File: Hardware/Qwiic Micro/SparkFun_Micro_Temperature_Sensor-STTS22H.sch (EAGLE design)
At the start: 27 parts, among them J1 Qwiic Right Angle, U2 STTS22H

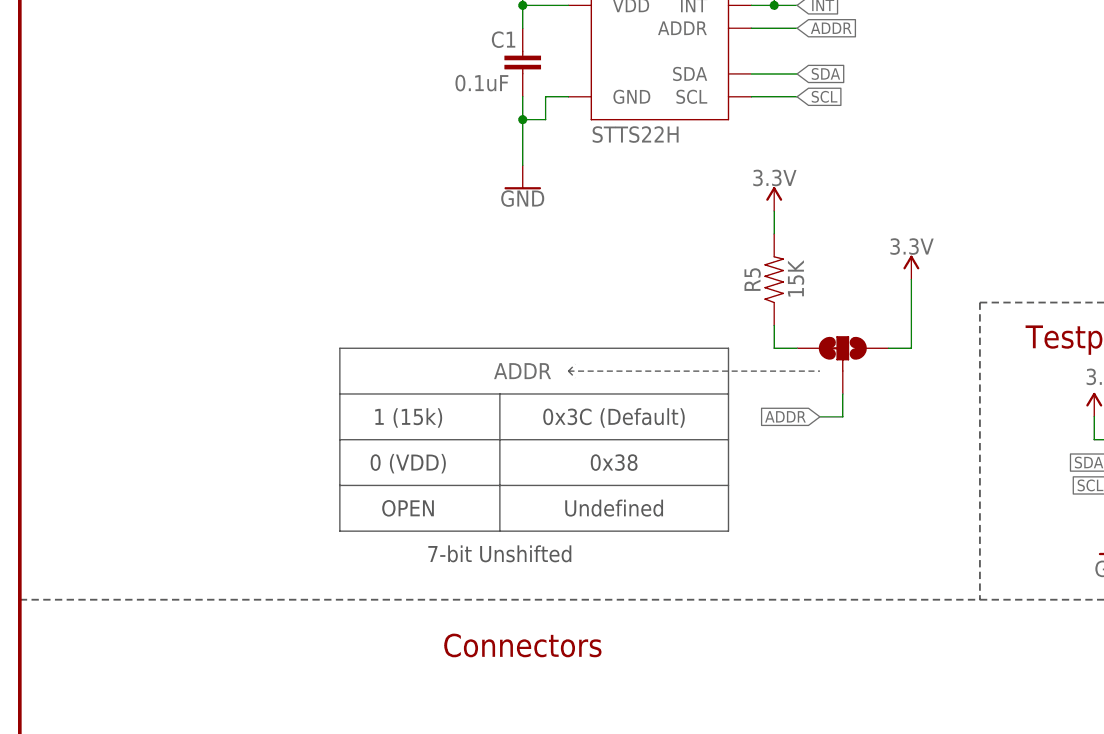
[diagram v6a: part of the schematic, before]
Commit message: Updates address selection text in schematic to be more clear
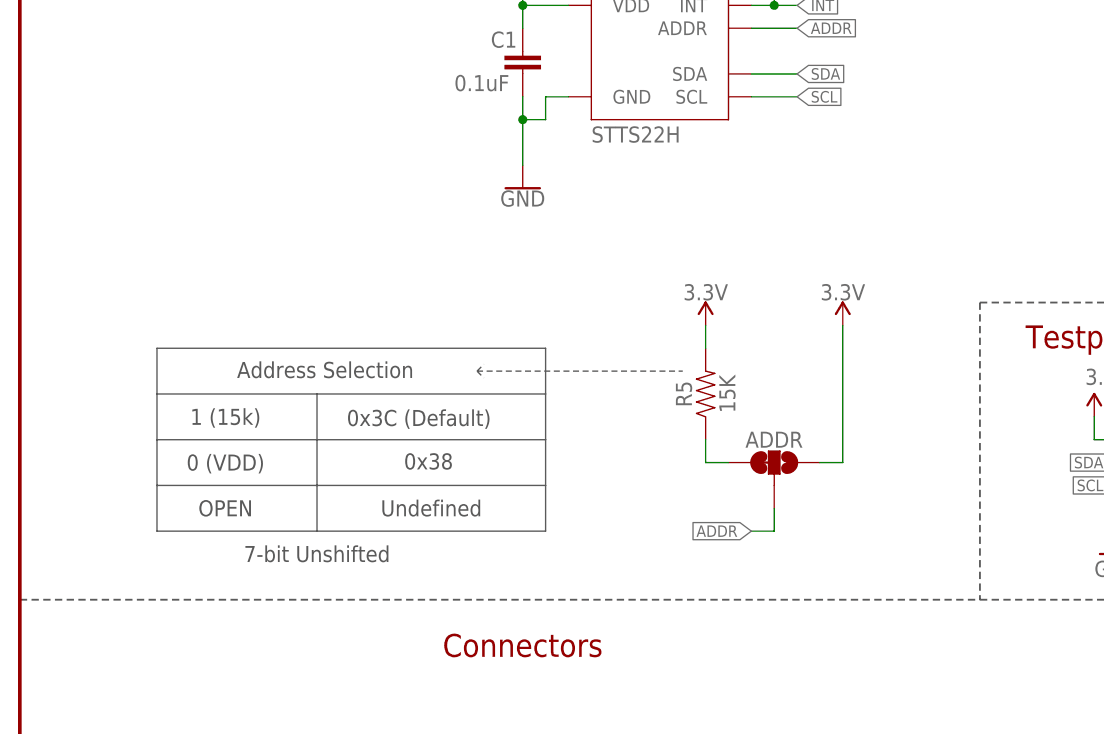
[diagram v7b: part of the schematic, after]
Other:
- note added: "Address Selection"
- moved on the sheet: ADDR, R5
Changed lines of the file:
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@@
 <text x="16.002" y="45.466" size="1.778" layer="97" font="vector">PTH connectors only
 accept 22AWG or smaller</text>
-<wire x1="35.56" y1="104.14" x2="35.56" y2="99.06" width="0.1524" layer="97"/>
-<wire x1="35.56" y1="99.06" x2="35.56" y2="93.98" width="0.1524" layer="97"/>
-<wire x1="35.56" y1="93.98" x2="35.56" y2="88.9" width="0.1524" layer="97"/>
-<wire x1="35.56" y1="88.9" x2="35.56" y2="83.82" width="0.1524" layer="97"/>
-<wire x1="53.34" y1="83.82" x2="78.74" y2="83.82" width="0.1524" layer="97"/>
-<wire x1="78.74" y1="83.82" x2="78.74" y2="88.9" width="0.1524" layer="97"/>
-<wire x1="78.74" y1="88.9" x2="78.74" y2="93.98" width="0.1524" layer="97"/>
-<wire x1="78.74" y1="93.98" x2="78.74" y2="99.06" width="0.1524" layer="97"/>
-<wire x1="78.74" y1="99.06" x2="78.74" y2="104.14" width="0.1524" layer="97"/>
-<wire x1="78.74" y1="104.14" x2="35.56" y2="104.14" width="0.1524" layer="97"/>
-<wire x1="35.56" y1="99.06" x2="53.34" y2="99.06" width="0.1524" layer="97"/>
-<wire x1="53.34" y1="99.06" x2="78.74" y2="99.06" width="0.1524" layer="97"/>
-<wire x1="53.34" y1="99.06" x2="53.34" y2="93.98" width="0.1524" layer="97"/>
-<wire x1="53.34" y1="93.98" x2="53.34" y2="88.9" width="0.1524" layer="97"/>
-<wire x1="53.34" y1="88.9" x2="53.34" y2="83.82" width="0.1524" layer="97"/>
-<wire x1="35.56" y1="88.9" x2="53.34" y2="88.9" width="0.1524" layer="97"/>
-<wire x1="35.56" y1="83.82" x2="53.34" y2="83.82" width="0.1524" layer="97"/>
-<wire x1="53.34" y1="88.9" x2="78.74" y2="88.9" width="0.1524" layer="97"/>
-<text x="43.18" y="96.52" size="1.778" layer="97" font="vector" align="center">1 (15k)</text>
-<text x="43.18" y="91.44" size="1.778" layer="97" font="vector" align="center">0 (VDD)</text>
-<text x="43.18" y="86.36" size="1.778" layer="97" font="vector" align="center">OPEN</text>
-<text x="66.04" y="86.36" size="1.778" layer="97" font="vector" align="center">Undefined</text>
-<text x="53.34" y="81.28" size="1.778" layer="97" font="vector" align="center">7-bit Unshifted</text>
-<wire x1="35.56" y1="93.98" x2="53.34" y2="93.98" width="0.1524" layer="97"/>
-<wire x1="53.34" y1="93.98" x2="78.74" y2="93.98" width="0.1524" layer="97"/>
-<text x="66.04" y="96.52" size="1.778" layer="97" font="vector" align="center">0x3C (Default)</text>
-<text x="66.04" y="91.44" size="1.778" layer="97" font="vector" align="center">0x38</text>
-<wire x1="60.96" y1="101.6" x2="88.9" y2="101.6" width="0.1524" layer="97" style="dashdot"/>
-<wire x1="60.96" y1="101.6" x2="61.722" y2="102.362" width="0.1524" layer="97" style="dashdot"/>
-<wire x1="60.96" y1="101.6" x2="61.722" y2="100.838" width="0.1524" layer="97" style="dashdot"/>
+<wire x1="15.24" y1="104.14" x2="15.24" y2="99.06" width="0.1524" layer="97"/>
+<wire x1="15.24" y1="99.06" x2="15.24" y2="93.98" width="0.1524" layer="97"/>
+<wire x1="15.24" y1="93.98" x2="15.24" y2="88.9" width="0.1524" layer="97"/>
+<wire x1="15.24" y1="88.9" x2="15.24" y2="83.82" width="0.1524" layer="97"/>
+<wire x1="33.02" y1="83.82" x2="58.42" y2="83.82" width="0.1524" layer="97"/>
+<wire x1="58.42" y1="83.82" x2="58.42" y2="88.9" width="0.1524" layer="97"/>
+<wire x1="58.42" y1="88.9" x2="58.42" y2="93.98" width="0.1524" layer="97"/>
+<wire x1="58.42" y1="93.98" x2="58.42" y2="99.06" width="0.1524" layer="97"/>
+<wire x1="58.42" y1="99.06" x2="58.42" y2="104.14" width="0.1524" layer="97"/>
+<wire x1="58.42" y1="104.14" x2="15.24" y2="104.14" width="0.1524" layer="97"/>
+<wire x1="15.24" y1="99.06" x2="33.02" y2="99.06" width="0.1524" layer="97"/>
+<wire x1="33.02" y1="99.06" x2="58.42" y2="99.06" width="0.1524" layer="97"/>
+<wire x1="33.02" y1="99.06" x2="33.02" y2="93.98" width="0.1524" layer="97"/>
+<wire x1="33.02" y1="93.98" x2="33.02" y2="88.9" width="0.1524" layer="97"/>
+<wire x1="33.02" y1="88.9" x2="33.02" y2="83.82" width="0.1524" layer="97"/>
+<wire x1="15.24" y1="88.9" x2="33.02" y2="88.9" width="0.1524" layer="97"/>
+<wire x1="15.24" y1="83.82" x2="33.02" y2="83.82" width="0.1524" layer="97"/>
+<wire x1="33.02" y1="88.9" x2="58.42" y2="88.9" width="0.1524" layer="97"/>
+<text x="22.86" y="96.52" size="1.778" layer="97" font="vector" align="center">1 (15k)</text>
+<text x="22.86" y="91.44" size="1.778" layer="97" font="vector" align="center">0 (VDD)</text>
+<text x="22.86" y="86.36" size="1.778" layer="97" font="vector" align="center">OPEN</text>
+<text x="45.72" y="86.36" size="1.778" layer="97" font="vector" align="center">Undefined</text>
+<text x="33.02" y="81.28" size="1.778" layer="97" font="vector" align="center">7-bit Unshifted</text>
+<wire x1="15.24" y1="93.98" x2="33.02" y2="93.98" width="0.1524" layer="97"/>
+<wire x1="33.02" y1="93.98" x2="58.42" y2="93.98" width="0.1524" layer="97"/>
+<text x="36.322" y="95.504" size="1.778" layer="97" font="vector" ratio="15">0x3C (Default)</text>
+<text x="42.672" y="90.678" size="1.778" layer="97" font="vector">0x38</text>
+<wire x1="50.8" y1="101.6" x2="73.66" y2="101.6" width="0.1524" layer="97" style="dashdot"/>
+<wire x1="50.8" y1="101.6" x2="51.562" y2="102.362" width="0.1524" layer="97" style="dashdot"/>
+<wire x1="50.8" y1="101.6" x2="51.562" y2="100.838" width="0.1524" layer="97" style="dashdot"/>
 <text x="68.58" y="177.8" size="2.54" layer="94" font="vector" align="center">Temperature Sensor - STTS22H</text>
+<text x="24.13" y="100.838" size="1.778" layer="97" font="vector">Address Selection</text>
 </plain>
 <instances>
@@
 <attribute name="VALUE" x="83.82" y="162.814" size="1.778" layer="96" font="vector" align="bottom-center"/>
 </instance>
-<instance part="ADDR" gate="G$1" x="91.44" y="104.14" smashed="yes" rot="MR90">
-<attribute name="NAME" x="55.88" y="101.6" size="1.778" layer="95" font="vector" rot="MR0" align="center"/>
-</instance>
-<instance part="SUPPLY8" gate="G$1" x="83.82" y="119.38" smashed="yes">
-<attribute name="VALUE" x="83.82" y="122.174" size="1.778" layer="96" font="vector" align="bottom-center"/>
+<instance part="ADDR" gate="G$1" x="83.82" y="91.44" smashed="yes" rot="MR90">
+<attribute name="NAME" x="83.82" y="93.98" size="1.778" layer="95" font="vector" rot="MR0" align="center"/>
+</instance>
+<instance part="SUPPLY8" gate="G$1" x="76.2" y="106.68" smashed="yes">
+<attribute name="VALUE" x="76.2" y="109.474" size="1.778" layer="96" font="vector" align="bottom-center"/>
 </instance>
 <instance part="C1" gate="G$1" x="55.88" y="134.62" smashed="yes">
@@
 <attribute name="VALUE" x="48.26" y="132.715" size="1.778" layer="96" font="vector"/>
 </instance>
-<instance part="R5" gate="G$1" x="83.82" y="111.76" smashed="yes" rot="R90">
-<attribute name="NAME" x="82.296" y="111.76" size="1.778" layer="95" font="vector" rot="R90" align="bottom-center"/>
-<attribute name="VALUE" x="85.344" y="111.76" size="1.778" layer="96" font="vector" rot="R90" align="top-center"/>
-</instance>
-<instance part="SUPPLY7" gate="G$1" x="99.06" y="111.76" smashed="yes">
-<attribute name="VALUE" x="99.06" y="114.554" size="1.778" layer="96" font="vector" align="bottom-center"/>
+<instance part="R5" gate="G$1" x="76.2" y="99.06" smashed="yes" rot="R90">
+<attribute name="NAME" x="74.676" y="99.06" size="1.778" layer="95" font="vector" rot="R90" align="bottom-center"/>
+<attribute name="VALUE" x="77.724" y="99.06" size="1.778" layer="96" font="vector" rot="R90" align="top-center"/>
+</instance>
+<instance part="SUPPLY7" gate="G$1" x="91.44" y="106.68" smashed="yes">
+<attribute name="VALUE" x="91.44" y="109.474" size="1.778" layer="96" font="vector" align="bottom-center"/>
 </instance>
 </instances>
@@
 <pinref part="R5" gate="G$1" pin="2"/>
 <pinref part="SUPPLY8" gate="G$1" pin="3.3V"/>
-<wire x1="83.82" y1="116.84" x2="83.82" y2="119.38" width="0.1524" layer="91"/>
+<wire x1="76.2" y1="104.14" x2="76.2" y2="106.68" width="0.1524" layer="91"/>
 </segment>
 <segment>
 <pinref part="ADDR" gate="G$1" pin="1"/>
-<wire x1="96.52" y1="104.14" x2="99.06" y2="104.14" width="0.1524" layer="91"/>
-<wire x1="99.06" y1="104.14" x2="99.06" y2="111.76" width="0.1524" layer="91"/>
+<wire x1="88.9" y1="91.44" x2="91.44" y2="91.44" width="0.1524" layer="91"/>
+<wire x1="91.44" y1="91.44" x2="91.44" y2="106.68" width="0.1524" layer="91"/>
 <pinref part="SUPPLY7" gate="G$1" pin="3.3V"/>
 </segment>
@@
 <segment>
 <pinref part="ADDR" gate="G$1" pin="2"/>
-<wire x1="91.44" y1="99.06" x2="91.44" y2="96.52" width="0.1524" layer="91"/>
-<wire x1="91.44" y1="96.52" x2="88.9" y2="96.52" width="0.1524" layer="91"/>
-<label x="88.9" y="96.52" size="1.27" layer="95" font="vector" rot="R180" xref="yes"/>
+<wire x1="83.82" y1="86.36" x2="83.82" y2="83.82" width="0.1524" layer="91"/>
+<wire x1="83.82" y1="83.82" x2="81.28" y2="83.82" width="0.1524" layer="91"/>
+<label x="81.28" y="83.82" size="1.27" layer="95" font="vector" rot="R180" xref="yes"/>
 </segment>
 </net>
@@
 <segment>
 <pinref part="ADDR" gate="G$1" pin="3"/>
-<wire x1="86.36" y1="104.14" x2="83.82" y2="104.14" width="0.1524" layer="91"/>
+<wire x1="78.74" y1="91.44" x2="76.2" y2="91.44" width="0.1524" layer="91"/>
 <pinref part="R5" gate="G$1" pin="1"/>
-<wire x1="83.82" y1="106.68" x2="83.82" y2="104.14" width="0.1524" layer="91"/>
-</segment>
-</net>
+<wire x1="76.2" y1="93.98" x2="76.2" y2="91.44" width="0.1524" layer="91"/>
+</segment>
+</net>
